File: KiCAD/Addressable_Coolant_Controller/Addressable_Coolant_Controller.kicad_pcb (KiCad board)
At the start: 2 copper layers, 210 x 176.5 mm, 66 parts, among them J1 XW4M-12D2-H1DA, J10 852-002-213R001, J11 852-002-213R001, J12 852-004-213R004, J2 XW4M-02D1-H1DA, J3 XW4M-12D2-H1DA, J4 852-002-213R001, J5 852-002-213R001, J6 852-002-213R001, J7 852-002-213R001, J8 852-002-213R001, J9 852-002-213R001, K1 G5V-1, K2 G5V-1, K3 G5V-1, K4 G5V-1, K5 G5V-1, K6 G5V-1, K7 G5V-1, K8 G5V-1, U1 PC12311NSZ1B, U10 ProS3, U2 PC12311NSZ1B, U3 PC12311NSZ1B, U4 PC12311NSZ1B, U5 PC12311NSZ1B, U6 PC12311NSZ1B, U7 PC12311NSZ1B, U8 PC12311NSZ1B, U9 PC12311NSZ1B

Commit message: Routed connector PCB and fixed components designators
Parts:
- removed R10: 2.28kΩ, Resistor:R_Axial_DIN0204_L3.6mm_D1.6mm_P5.08mm_Horizontal-JW
- removed R12, R14, R16, R18: 210Ω, Resistor:R_Axial_DIN0204_L3.6mm_D1.6mm_P5.08mm_Horizontal-JW
- removed R13, R15, R17: 1.1kΩ, Resistor:R_Axial_DIN0204_L3.6mm_D1.6mm_P5.08mm_Horizontal-JW
- added R22: 210Ω, Resistor:R_Axial_DIN0204_L3.6mm_D1.6mm_P5.08mm_Horizontal-JW, F.Cu at (92.5, 66.5)
- added R33: 210Ω, Resistor:R_Axial_DIN0204_L3.6mm_D1.6mm_P5.08mm_Horizontal-JW, F.Cu at (106.7, 66.5)
- added R44: 210Ω, Resistor:R_Axial_DIN0204_L3.6mm_D1.6mm_P5.08mm_Horizontal-JW, F.Cu at (120.9, 66.5)
- added R55: 210Ω, Resistor:R_Axial_DIN0204_L3.6mm_D1.6mm_P5.08mm_Horizontal-JW, F.Cu at (135.1, 66.5)
- added R66: 210Ω, Resistor:R_Axial_DIN0204_L3.6mm_D1.6mm_P5.08mm_Horizontal-JW, F.Cu at (149.3, 66.5)
- added R77: 210Ω, Resistor:R_Axial_DIN0204_L3.6mm_D1.6mm_P5.08mm_Horizontal-JW, F.Cu at (163.5, 66.5)
- added R88: 210Ω, Resistor:R_Axial_DIN0204_L3.6mm_D1.6mm_P5.08mm_Horizontal-JW, F.Cu at (177.7, 66.5)
- added R99: 2.28kΩ, Resistor:R_Axial_DIN0204_L3.6mm_D1.6mm_P5.08mm_Horizontal-JW, F.Cu at (176.4, 169.8)
- J1: value XW4M-12D2-H1DA -> 852-002-213R001; footprint xw4m-12d2-h1da:xw4m-12d2-h1da -> 852-002-213R001:852-002-213R001
- J10: value 852-002-213R001 -> XW4M-12D2-H1DA; footprint 852-002-213R001:852-002-213R001 -> xw4m-12d2-h1da:xw4m-12d2-h1da
- J11: value 852-002-213R001 -> XW4M-12D2-H1DA; footprint 852-002-213R001:852-002-213R001 -> xw4m-12d2-h1da:xw4m-12d2-h1da; moved to B.Cu
- J12: value 852-004-213R004 -> XW4M-02D1-H1DA; footprint 852-002-213R004:852004213R004 -> xw4m-02d1-h1da:xw4m-02d1-h1da
- J2: value XW4M-02D1-H1DA -> 852-002-213R001; footprint xw4m-02d1-h1da:xw4m-02d1-h1da -> 852-002-213R001:852-002-213R001
- J3: value XW4M-12D2-H1DA -> 852-002-213R001; footprint xw4m-12d2-h1da:xw4m-12d2-h1da -> 852-002-213R001:852-002-213R001; moved to F.Cu
- J9: value 852-002-213R001 -> 852-004-213R004; footprint 852-002-213R001:852-002-213R001 -> 852-002-213R004:852004213R004
- LED5: value C503B-GCN -> C503B-BCN; footprint CreeLED Green:C503B_GCN_CY0C0792 -> CreeLED Blue:C503B_BCN_CV0Z0461
- LED9: value C503B-BCN -> C503B-GCN; footprint CreeLED Blue:C503B_BCN_CV0Z0461 -> CreeLED Green:C503B_GCN_CY0C0792
- R11: value 1.1kΩ -> 210Ω
- R2, R4, R6, R8: value 210Ω -> 1.1kΩ
- moved J10 213.0 mm to (121.3, 190.3)
- moved J1 201.4 mm to (266.7, 47.7), turned to -90 degrees
- moved J2 162.8 mm to (266.7, 65.5), turned to -90 degrees
- moved J9 138.1 mm to (266.7, 190.0), turned to -90 degrees
- moved J11 130.2 mm to (275.5, 201.1), turned to 180 degrees
- moved J3 118.0 mm to (266.7, 83.3), turned to -90 degrees
- moved J8 117.1 mm to (266.7, 172.2), turned to -90 degrees
- moved R9 113.6 mm to (182.4, 169.8), turned to -90 degrees
- moved J6 101.9 mm to (266.7, 136.6), turned to -90 degrees
- moved J12 101.3 mm to (165.5, 192.7), turned to 0 degrees
- moved J7 96.3 mm to (266.7, 154.4), turned to -90 degrees
- moved J5 80.7 mm to (266.7, 118.9), turned to -90 degrees
- moved R11 71.0 mm to (78.3, 66.5)
- moved J4 59.5 mm to (266.7, 101.1), turned to -90 degrees
- moved R8 56.9 mm to (183.0, 75.3)
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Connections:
- J1 pad 1: /Main_Board/S1 -> /Connector_Board/S1
- J1 pad 3: /Main_Board/S5 -> /Connector_Board/GND
- J10 pad 1: /Connector_Board/S7 -> /Main_Board/S1
- J10 pad 3: /Connector_Board/GND -> /Main_Board/S5
- J11 pad 1: /Connector_Board/S8 -> /Connector_Board/S1
- J11 pad 3: /Connector_Board/GND -> /Connector_Board/S5
- J12 pad 1: /Connector_Board/MCU 3.3v -> +24V
- J12 pad 2: /Connector_Board/PS Out -> GND
- J12 pad 3: /Connector_Board/MCU GND -> (no net)
- J12 pad 4: unconnected-(J12-Pad4) -> (no net)
- J2 pad 1: +24V -> /Connector_Board/S2
- J2 pad 3: (no net) -> /Connector_Board/GND
- J3 pad 1: /Connector_Board/S1 -> /Connector_Board/S3
- J3 pad 3: /Connector_Board/S5 -> /Connector_Board/GND
- J4 pad 1: /Connector_Board/S1 -> /Connector_Board/S4
- J5 pad 1: /Connector_Board/S2 -> /Connector_Board/S5
- J6 pad 1: /Connector_Board/S3 -> /Connector_Board/S6
- J7 pad 1: /Connector_Board/S4 -> /Connector_Board/S7
- J8 pad 1: /Connector_Board/S5 -> /Connector_Board/S8
- J9 pad 1: /Connector_Board/S6 -> /Connector_Board/MCU 3.3v
- J9 pad 3: /Connector_Board/GND -> /Connector_Board/MCU GND
- K1 pad 5: /Main_Board/S8 -> /Main_Board/S1
- K1 pad 6: /Main_Board/S8 -> /Main_Board/S1
- K2 pad 5: /Main_Board/S6 -> /Main_Board/S2
- K2 pad 6: /Main_Board/S6 -> /Main_Board/S2
- K3 pad 5: /Main_Board/S4 -> /Main_Board/S3
- K3 pad 6: /Main_Board/S4 -> /Main_Board/S3
- K4 pad 5: /Main_Board/S3 -> /Main_Board/S4
- K4 pad 6: /Main_Board/S3 -> /Main_Board/S4
- K5 pad 5: /Main_Board/S2 -> /Main_Board/S5
- K5 pad 6: /Main_Board/S2 -> /Main_Board/S5
- K6 pad 5: /Main_Board/S1 -> /Main_Board/S6
- K6 pad 6: /Main_Board/S1 -> /Main_Board/S6
- K7 pad 5: /Main_Board/S5 -> /Main_Board/S7
- K7 pad 6: /Main_Board/S5 -> /Main_Board/S7
- K8 pad 5: /Main_Board/S7 -> /Main_Board/S8
- K8 pad 6: /Main_Board/S7 -> /Main_Board/S8
- R11 pad 1: Net-(LED6-Pad1) -> /Main_Board/MCU 3.3v
- R11 pad 2: Net-(D5-A) -> Net-(R11-Pad2)
- R2 pad 1: /Main_Board/MCU 3.3v -> Net-(LED2-Pad1)
- R2 pad 2: Net-(R2-Pad2) -> Net-(D2-A)
- R3 pad 1: Net-(LED2-Pad1) -> Net-(LED3-Pad1)
- R3 pad 2: Net-(D2-A) -> Net-(D3-A)
- R4 pad 1: /Main_Board/MCU 3.3v -> Net-(LED4-Pad1)
- R4 pad 2: Net-(R4-Pad2) -> Net-(D4-A)
- R5 pad 1: Net-(LED3-Pad1) -> Net-(LED5-Pad1)
- R5 pad 2: Net-(D3-A) -> Net-(D5-A)
- R6 pad 1: /Main_Board/MCU 3.3v -> Net-(LED6-Pad1)
- R6 pad 2: Net-(R6-Pad2) -> Net-(D6-A)
- R7 pad 1: Net-(LED4-Pad1) -> Net-(LED7-Pad1)
- R7 pad 2: Net-(D4-A) -> Net-(D7-A)
- R8 pad 1: /Main_Board/MCU 3.3v -> Net-(LED8-Pad1)
- R8 pad 2: Net-(R8-Pad2) -> Net-(D8-A)
- R9 pad 1: Net-(LED5-Pad1) -> Net-(LED9-Pad1)
- U1 pad 1: Net-(R14-Pad2) -> Net-(R11-Pad2)
- U1 pad 4: Net-(D6-A) -> Net-(D1-A)
- U2 pad 4: Net-(D5-A) -> Net-(D2-A)
- U3 pad 1: Net-(R8-Pad2) -> Net-(R33-Pad2)
- U3 pad 4: Net-(D4-A) -> Net-(D3-A)
- U4 pad 1: Net-(R6-Pad2) -> Net-(R44-Pad2)
- U4 pad 4: Net-(D3-A) -> Net-(D4-A)
- U5 pad 4: Net-(D7-A) -> Net-(D5-A)
- U6 pad 1: Net-(R4-Pad2) -> Net-(R66-Pad2)
- U6 pad 4: Net-(D2-A) -> Net-(D6-A)
- U7 pad 4: Net-(D8-A) -> Net-(D7-A)
- U8 pad 1: Net-(R2-Pad2) -> Net-(R88-Pad2)
- U8 pad 4: Net-(D1-A) -> Net-(D8-A)
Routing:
- net (no net): track 1041.2 -> 0.00 mm
- net +24V: track 480.2 -> 1221.3 mm
- net /Main_Board/MCU 3.3v: track 10.9 -> 351.0 mm
- net Net-(D8-A): track 55.8 -> 223.4 mm
- net /Connector_Board/S1: track 0.00 -> 160.7 mm
- net Net-(D7-A): track 64.6 -> 223.4 mm
- net Net-(D4-A): track 64.6 -> 223.4 mm
- net Net-(D3-A): track 64.6 -> 223.4 mm
- net Net-(D5-A): track 64.6 -> 223.4 mm
- net Net-(D6-A): track 64.6 -> 223.4 mm
- net /Connector_Board/GND: track 0.00 -> 158.5 mm
- net Net-(D2-A): track 65.0 -> 223.4 mm
- net /Connector_Board/S2: track 0.00 -> 145.6 mm
- net /Connector_Board/S3: track 0.00 -> 124.3 mm
- net /Main_Board/S8: track 0.00 -> 115.2 mm
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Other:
- board text added: "Addressable Coolant Controller v1.0.0 Warner Consulting Inc. Josh Warner 11/25/2024"
- board text removed: "Addressable Coolant Controller v1.0.0 Warner Consulting Inc. Josh Warner 10/29/2024"

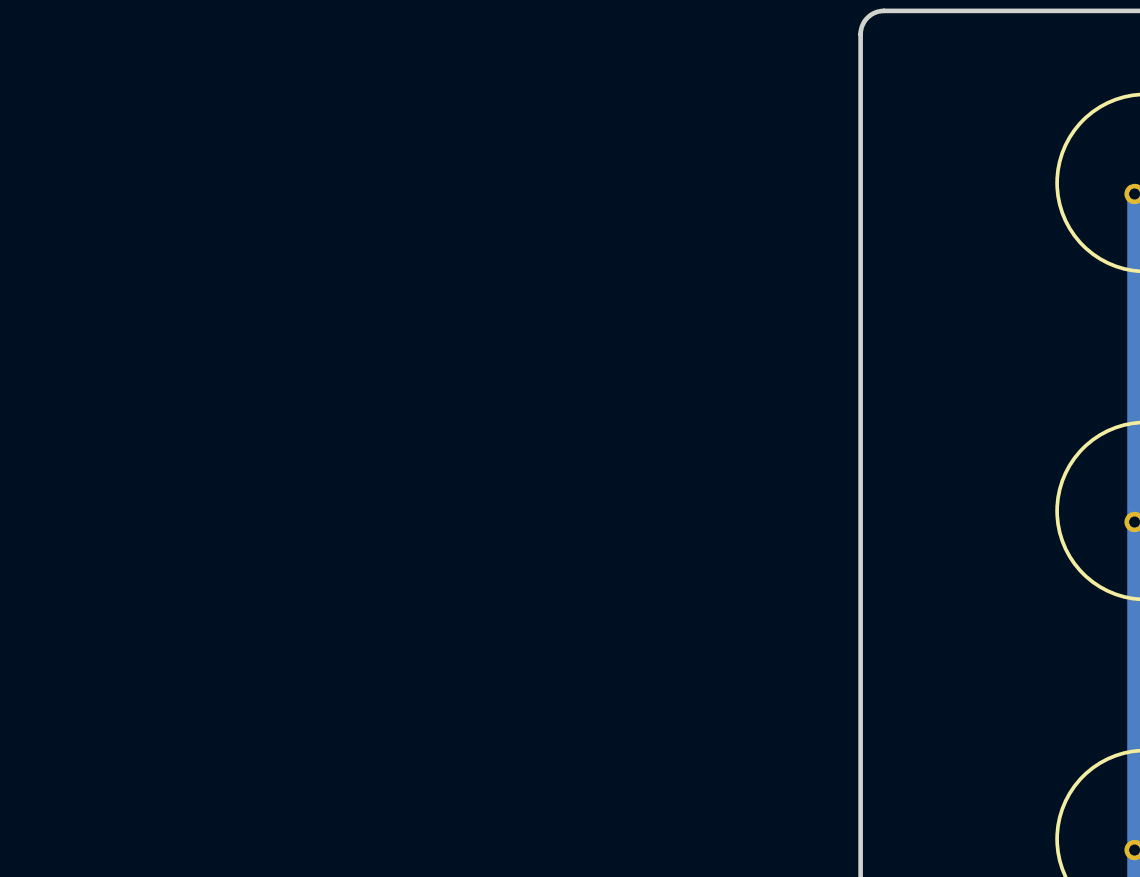
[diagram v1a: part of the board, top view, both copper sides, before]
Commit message: Added LEDs to connector board, and moved to hierarchical sheet
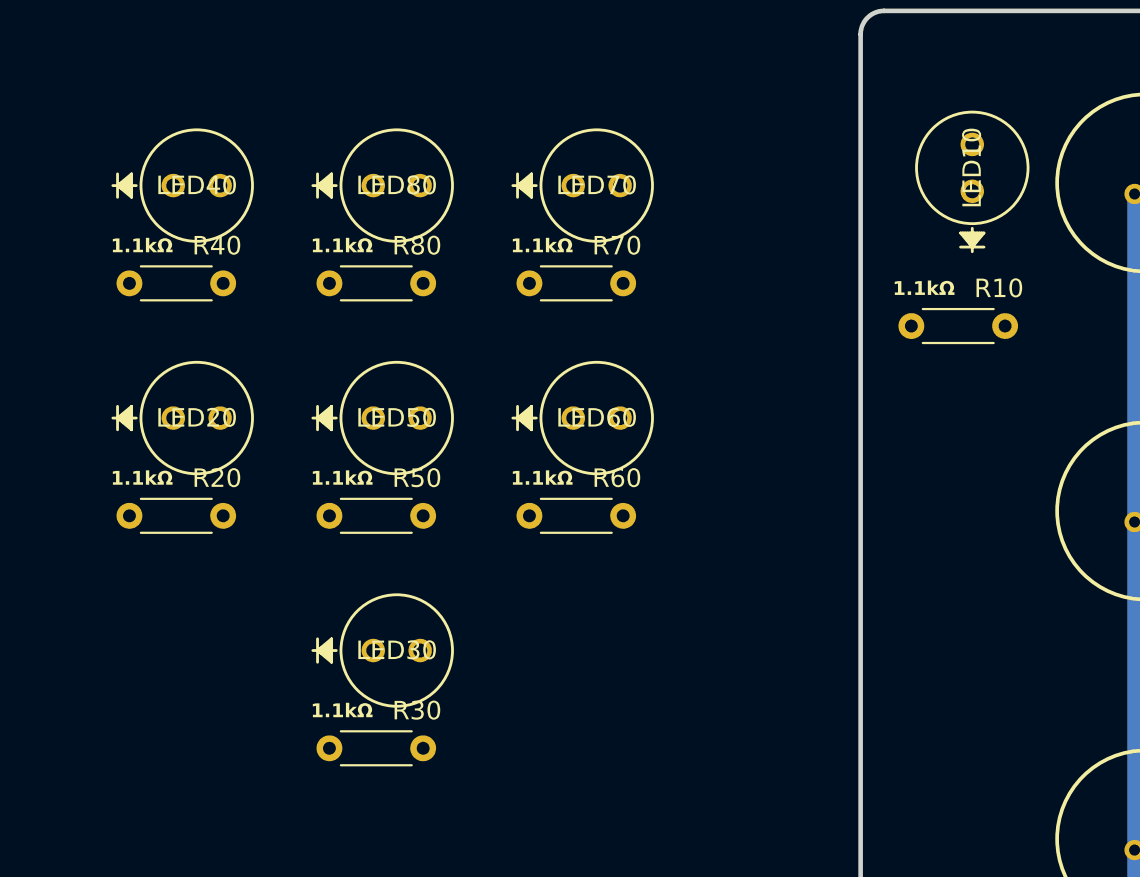
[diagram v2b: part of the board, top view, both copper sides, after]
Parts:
- added LED10: C503B-BCN, CreeLED Blue:C503B_BCN_CV0Z0461, F.Cu at (257.3, 48.2)
- added LED20: C503B-BCN, CreeLED Blue:C503B_BCN_CV0Z0461, F.Cu at (214.0, 60.5)
- added LED30: C503B-BCN, CreeLED Blue:C503B_BCN_CV0Z0461, F.Cu at (224.8, 73.1)
- added LED40: C503B-BCN, CreeLED Blue:C503B_BCN_CV0Z0461, F.Cu at (214.0, 47.9)
- added LED50: C503B-BCN, CreeLED Blue:C503B_BCN_CV0Z0461, F.Cu at (224.8, 60.5)
- added LED60: C503B-BCN, CreeLED Blue:C503B_BCN_CV0Z0461, F.Cu at (235.7, 60.5)
- added LED70: C503B-BCN, CreeLED Blue:C503B_BCN_CV0Z0461, F.Cu at (235.7, 47.9)
- added LED80: C503B-BCN, CreeLED Blue:C503B_BCN_CV0Z0461, F.Cu at (224.8, 47.9)
- added R10: 1.1kΩ, Resistor:R_Axial_DIN0204_L3.6mm_D1.6mm_P5.08mm_Horizontal-JW, F.Cu at (254.0, 55.5)
- added R20: 1.1kΩ, Resistor:R_Axial_DIN0204_L3.6mm_D1.6mm_P5.08mm_Horizontal-JW, F.Cu at (211.6, 65.8)
- added R30: 1.1kΩ, Resistor:R_Axial_DIN0204_L3.6mm_D1.6mm_P5.08mm_Horizontal-JW, F.Cu at (222.5, 78.4)
- added R40: 1.1kΩ, Resistor:R_Axial_DIN0204_L3.6mm_D1.6mm_P5.08mm_Horizontal-JW, F.Cu at (211.6, 53.2)
- added R50: 1.1kΩ, Resistor:R_Axial_DIN0204_L3.6mm_D1.6mm_P5.08mm_Horizontal-JW, F.Cu at (222.5, 65.8)
- added R60: 1.1kΩ, Resistor:R_Axial_DIN0204_L3.6mm_D1.6mm_P5.08mm_Horizontal-JW, F.Cu at (233.3, 65.8)
- added R70: 1.1kΩ, Resistor:R_Axial_DIN0204_L3.6mm_D1.6mm_P5.08mm_Horizontal-JW, F.Cu at (233.3, 53.2)
- added R80: 1.1kΩ, Resistor:R_Axial_DIN0204_L3.6mm_D1.6mm_P5.08mm_Horizontal-JW, F.Cu at (222.5, 53.2)

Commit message: Updating Cree LED footprints with STEP files
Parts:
- LED1, LED2, LED3, LED4, LED5, LED6, LED7, LED8: footprint CreeLED Blue:C503B_BCN_CV0Z0461 -> C503B_BCN_CV0Z0461:C503B_BCN_CV0Z0461
- LED10, LED20, LED30, LED40, LED50, LED60, LED70, LED80: footprint CreeLED Blue:C503B_BCN_CV0Z0461 -> C503B_BCN_CV0Z0461:C503B_BCN_CV0Z0461; moved to B.Cu
- LED9: footprint CreeLED Green:C503B_GCN_CY0C0792 -> C503B_GCN_CY0C0792:C503B_GCN_CY0C0792
- moved R80 130.6 mm to (254.0, 180.0)
- moved LED80 128.3 mm to (256.5, 172.2), turned to -90 degrees
- moved R70 110.2 mm to (254.0, 161.4)
- moved LED70 107.8 mm to (256.5, 153.7), turned to -90 degrees
- moved R60 81.3 mm to (254.0, 144.4)
- moved LED60 79.0 mm to (256.5, 136.6), turned to -90 degrees
- moved R40 70.0 mm to (254.0, 108.8)
- moved R50 68.5 mm to (254.0, 126.6)
- moved LED40 68.1 mm to (256.5, 101.1), turned to -90 degrees
- moved LED50 66.4 mm to (256.5, 118.9), turned to -90 degrees
- moved R20 43.0 mm to (254.0, 73.3)
- moved LED20 42.8 mm to (256.5, 65.5), turned to -90 degrees
- moved R30 34.0 mm to (254.0, 91.1)
- moved LED30 33.3 mm to (256.5, 83.3), turned to -90 degrees
- moved LED10 0.89 mm to (256.5, 47.7), turned to -90 degrees
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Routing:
- net /Connector_Board/GND: track 158.5 -> 239.1 mm
- net /Connector_Board/S8: track 37.0 -> 48.5 mm
- net /Connector_Board/S7: track 51.9 -> 63.4 mm
- net /Connector_Board/S5: track 88.1 -> 99.6 mm
- net /Connector_Board/S4: track 109.3 -> 120.8 mm
- net /Connector_Board/S3: track 124.3 -> 135.9 mm
- net /Connector_Board/S6: track 73.1 -> 84.6 mm
- net /Connector_Board/S2: track 145.6 -> 157.2 mm
- net /Connector_Board/S1: track 160.7 -> 172.3 mm
- net Net-(LED80-Pad1): track 0.00 -> 10.1 mm
- net Net-(LED70-Pad1): track 0.00 -> 10.1 mm
- net Net-(LED60-Pad1): track 0.00 -> 10.1 mm
- net Net-(LED10-Pad1): track 0.00 -> 10.1 mm
- net Net-(LED50-Pad1): track 0.00 -> 10.1 mm
- net Net-(LED40-Pad1): track 0.00 -> 10.1 mm
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- added copper zone on B.Cu, net /Connector_Board/GND
- added copper zone on F.Cu, net /Connector_Board/MCU GND

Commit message: Updating PC123 footprint with STEP file
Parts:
- R10, R20, R30, R40, R50, R60, R70, R80: moved to B.Cu

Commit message: Finished board layout
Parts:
- added Connector_Board: Board, PCM_kikit:Board, F.Cu at (254.8, 38.4)
- added Main_Board: Board, PCM_kikit:Board, F.Cu at (78.5, 44.6)
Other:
- board text added: "Addressable Coolant Controller v1.0.0 Warner Consulting Inc. Josh Warner 11/26/2024"
- board text removed: "Addressable Coolant Controller v1.0.0 Warner Consulting Inc. Josh Warner 11/25/2024"
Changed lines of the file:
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@@
     (38 "B.Mask" user)
     (39 "F.Mask" user)
+    (40 "Dwgs.User" user "User.Drawings")
     (44 "Edge.Cuts" user)
     (45 "Margin" user)
@@
     (pad "4" thru_hole circle (at 3.81 -1.27 180) (size 1.1 1.1) (drill 0.7) (layers "*.Cu" "*.Mask")
       (net 8 "Net-(D7-A)") (pintype "passive"))
-    (model "PC12311NSZ1B.stp"
+    (model "C:/Users/Josh/Dropbox/JOSHUA/Warner Consulting/Collet Autofeed/Warner-Consulting-Libraries/PC12311NSZ1B/PC12311NSZ1B Step/PC12311NSZ1B.stp"
       (offset (xyz 0 0 0))
       (scale (xyz 1 1 1))
@@
     (pad "4" thru_hole circle (at 3.81 -1.27 180) (size 1.1 1.1) (drill 0.7) (layers "*.Cu" "*.Mask")
       (net 9 "Net-(D8-A)") (pintype "passive"))
-    (model "PC12311NSZ1B.stp"
+    (model "C:/Users/Josh/Dropbox/JOSHUA/Warner Consulting/Collet Autofeed/Warner-Consulting-Libraries/PC12311NSZ1B/PC12311NSZ1B Step/PC12311NSZ1B.stp"
       (offset (xyz 0 0 0))
       (scale (xyz 1 1 1))
@@
     (pad "4" thru_hole circle (at 3.81 -1.27 180) (size 1.1 1.1) (drill 0.7) (layers "*.Cu" "*.Mask")
       (net 7 "Net-(D6-A)") (pintype "passive"))
-    (model "PC12311NSZ1B.stp"
+    (model "C:/Users/Josh/Dropbox/JOSHUA/Warner Consulting/Collet Autofeed/Warner-Consulting-Libraries/PC12311NSZ1B/PC12311NSZ1B Step/PC12311NSZ1B.stp"
       (offset (xyz 0 0 0))
       (scale (xyz 1 1 1))
@@
     (pad "4" thru_hole circle (at 3.81 -1.27 180) (size 1.1 1.1) (drill 0.7) (layers "*.Cu" "*.Mask")
       (net 2 "Net-(D1-A)") (pintype "passive"))
-    (model "PC12311NSZ1B.stp"
+    (model "C:/Users/Josh/Dropbox/JOSHUA/Warner Consulting/Collet Autofeed/Warner-Consulting-Libraries/PC12311NSZ1B/PC12311NSZ1B Step/PC12311NSZ1B.stp"
       (offset (xyz 0 0 0))
       (scale (xyz 1 1 1))
@@
     (pad "4" thru_hole circle (at 3.81 -1.27 180) (size 1.1 1.1) (drill 0.7) (layers "*.Cu" "*.Mask")
       (net 3 "Net-(D2-A)") (pintype "passive"))
-    (model "PC12311NSZ1B.stp"
+    (model "C:/Users/Josh/Dropbox/JOSHUA/Warner Consulting/Collet Autofeed/Warner-Consulting-Libraries/PC12311NSZ1B/PC12311NSZ1B Step/PC12311NSZ1B.stp"
       (offset (xyz 0 0 0))
       (scale (xyz 1 1 1))
@@
     (pad "4" thru_hole circle (at 3.81 -1.27 180) (size 1.1 1.1) (drill 0.7) (layers "*.Cu" "*.Mask")
       (net 5 "Net-(D4-A)") (pintype "passive"))
-    (model "PC12311NSZ1B.stp"
+    (model "C:/Users/Josh/Dropbox/JOSHUA/Warner Consulting/Collet Autofeed/Warner-Consulting-Libraries/PC12311NSZ1B/PC12311NSZ1B Step/PC12311NSZ1B.stp"
       (offset (xyz 0 0 0))
       (scale (xyz 1 1 1))
@@
     )
   )
+  (footprint "PCM_kikit:Board" (layer "F.Cu")
+    (at 254.762 38.4175)
+    (descr "Mark board for extraction")
+    (attr board_only exclude_from_pos_files exclude_from_bom allow_missing_courtyard)
+    (fp_text reference "Connector_Board" (at -4.5 -5) (layer "Dwgs.User")
+        (effects (font (size 1 1) (thickness 0.15)) (justify left))
+    )
+    (fp_text value "Board" (at -7.25 -5) (layer "Dwgs.User")
+        (effects (font (size 1 1) (thickness 0.15)))
+    )
+    (fp_line (start -1.25 -4) (end -9.25 -4)
+      (stroke (width 0.2) (type solid)) (layer "Dwgs.User"))
+    (fp_line (start 0 0) (end -1.25 -4)
+      (stroke (width 0.2) (type solid)) (layer "Dwgs.User"))
+    (fp_line (start 0 0) (end -1 -0.5)
+      (stroke (width 0.2) (type solid)) (layer "Dwgs.User"))
+    (fp_line (start 0 0) (end 0.5 -1)
+      (stroke (width 0.2) (type solid)) (layer "Dwgs.User"))
+  )
   (footprint "PC12311NSZ1B:PC12311NSZ1B" (layer "F.Cu")
     (at 109.2385 57.023 180)
@@
     (pad "4" thru_hole circle (at 3.81 -1.27 180) (size 1.1 1.1) (drill 0.7) (layers "*.Cu" "*.Mask")
       (net 4 "Net-(D3-A)") (pintype "passive"))
-    (model "PC12311NSZ1B.stp"
+    (model "C:/Users/Josh/Dropbox/JOSHUA/Warner Consulting/Collet Autofeed/Warner-Consulting-Libraries/PC12311NSZ1B/PC12311NSZ1B Step/PC12311NSZ1B.stp"
       (offset (xyz 0 0 0))
       (scale (xyz 1 1 1))
@@
     (pad "4" thru_hole circle (at 3.81 -1.27 180) (size 1.1 1.1) (drill 0.7) (layers "*.Cu" "*.Mask")
       (net 32 "/Main_Board/MCU 3.3v") (pintype "passive"))
-    (model "PC12311NSZ1B.stp"
+    (model "C:/Users/Josh/Dropbox/JOSHUA/Warner Consulting/Collet Autofeed/Warner-Consulting-Libraries/PC12311NSZ1B/PC12311NSZ1B Step/PC12311NSZ1B.stp"
       (offset (xyz 0 0 0))
       (scale (xyz 1 1 1))
@@
     (pad "4" thru_hole circle (at 3.81 -1.27 180) (size 1.1 1.1) (drill 0.7) (layers "*.Cu" "*.Mask")
       (net 6 "Net-(D5-A)") (pintype "passive"))
-    (model "PC12311NSZ1B.stp"
+    (model "C:/Users/Josh/Dropbox/JOSHUA/Warner Consulting/Collet Autofeed/Warner-Consulting-Libraries/PC12311NSZ1B/PC12311NSZ1B Step/PC12311NSZ1B.stp"
       (offset (xyz 0 0 0))
       (scale (xyz 1 1 1))
@@
     )
   )
+  (footprint "PCM_kikit:Board" (layer "F.Cu")
+    (at 78.486 44.61056)
+    (descr "Mark board for extraction")
+    (attr board_only exclude_from_pos_files exclude_from_bom allow_missing_courtyard)
+    (fp_text reference "Main_Board" (at -4.5 -5) (layer "Dwgs.User")
+        (effects (font (size 1 1) (thickness 0.15)) (justify left))
+    )
+    (fp_text value "Board" (at -7.25 -5) (layer "Dwgs.User")
+        (effects (font (size 1 1) (thickness 0.15)))
+    )
+    (fp_line (start -1.25 -4) (end -9.25 -4)
+      (stroke (width 0.2) (type solid)) (layer "Dwgs.User"))
+    (fp_line (start 0 0) (end -1.25 -4)
+      (stroke (width 0.2) (type solid)) (layer "Dwgs.User"))
+    (fp_line (start 0 0) (end -1 -0.5)
+      (stroke (width 0.2) (type solid)) (layer "Dwgs.User"))
+    (fp_line (start 0 0) (end 0.5 -1)
+      (stroke (width 0.2) (type solid)) (layer "Dwgs.User"))
+  )
   (footprint "852-002-213R001:852-002-213R001" (layer "F.Cu")
     (at 266.7 101.0824 -90)
@@
     (effects (font (size 2 2) (thickness 0.25)) (justify right))
   )
-  (gr_text "Addressable Coolant Controller v1.0.0\nWarner Consulting Inc.\nJosh Warner\n11/25/2024" (at 107.93236 187.61256) (layer "F.SilkS")
+  (gr_text "Addressable Coolant Controller v1.0.0\nWarner Consulting Inc.\nJosh Warner\n11/26/2024" (at 107.93236 187.61256) (layer "F.SilkS")
     (effects (font (size 1.5 1.5) (thickness 0.15)) (justify left bottom))
   )
